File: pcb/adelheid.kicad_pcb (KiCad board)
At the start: 2 copper layers, 339.1 x 143.2 mm, 323 parts, among them J1 USB_B_Mini, J12 VCC, J13 D+, J14 D-, J15 GND, J2 MISO, J3 VCC, J4 SCK, J5 MOSI, J6 RES, J7 GND, J8 PF4, J9 PF5, Q1 2N7002, U1 USBLC6-2SC6, U2 ATmega32U4-AU, Y1 Crystal_GND24

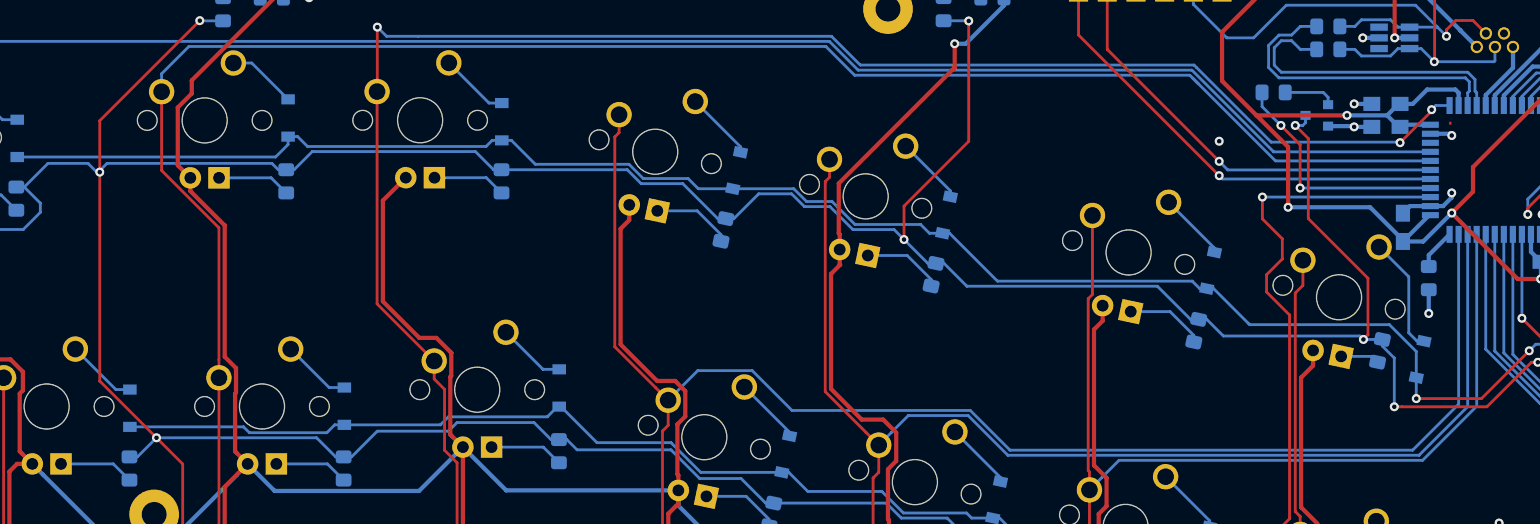
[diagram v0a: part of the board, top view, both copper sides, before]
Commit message: switched backlight pin [Rev2.0]
swapped col4 and led pin.
Backlight is now on pin 31 (C6).
In Rev1.0 the backlight started flickering because the MCU couldn't
handle the load of the LEDs on pin 37. This should fix the issue.
Thank you u/SryImBadAtNaming for finding out and notifying me!
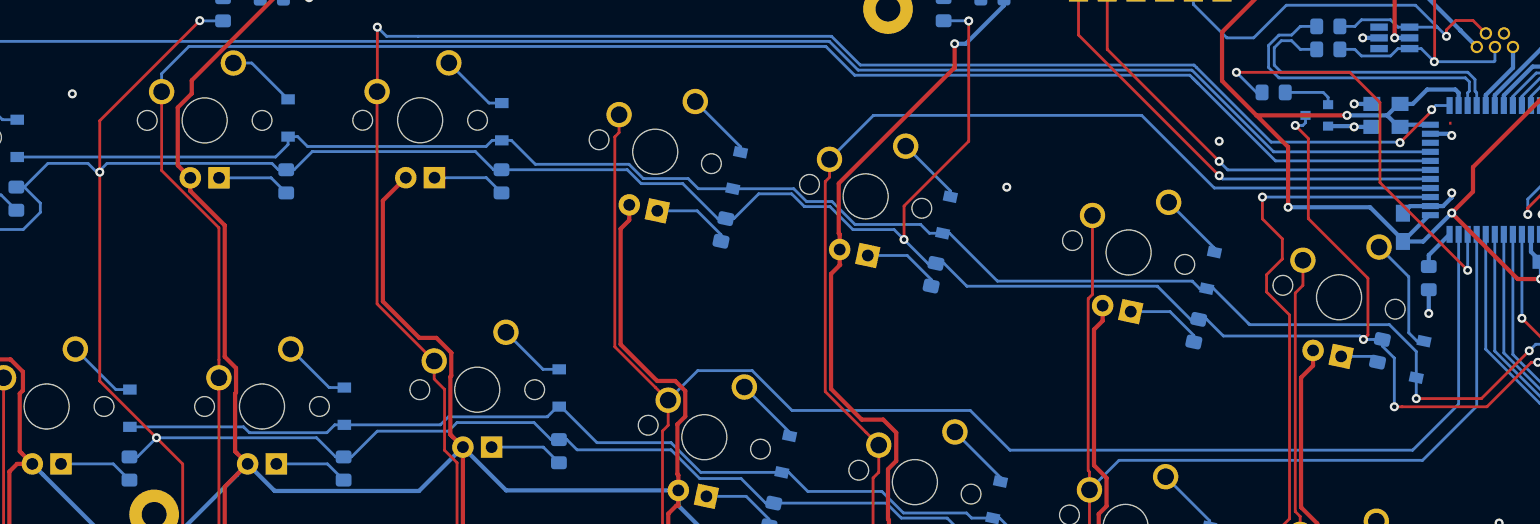
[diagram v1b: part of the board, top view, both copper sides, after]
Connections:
- U2 pad 31: /col4 -> Net-(R5-Pad1)
- U2 pad 37: Net-(R5-Pad1) -> /col4
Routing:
- net Net-(R5-Pad1): track 21.6 -> 38.0 mm
- net /col4: track 187.7 -> 173.5 mm
- net GND: vias 19 -> 21
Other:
- board text added: "fork of FateNozomi/arisu-pcb by floookay [Rev2.0]"
- board text removed: "fork of FateNozomi/arisu-pcb by floookay [Rev1.0]"
